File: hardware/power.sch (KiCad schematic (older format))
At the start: 39 parts, among them U200 SY8089AAC, U220 PAM2305CGFADJ, U230 PAM2305CGFADJ, U250 PAM2305CGFADJ, U260 NCP707_XDFN4

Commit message: wip
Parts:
- added L251: 2.2u,0806, require:L_0806, symbol Device:L
- C201, C221, C231: value 10u -> 10u,10V; footprint require:C_0603 -> require:C_0805
- C202, C222, C232, C252: value 22p -> 100p
- C210: value 0.1u -> 10n
- C223, C233: value 22u -> 10u
- C251: value 2.2u,10V -> 10u,10V; footprint require:C_0603 -> require:C_0805
- C253: value 22u -> 10u,10V; footprint require:C_0603 -> require:C_0805
- L230: value 0.47u,3A -> 2.2u
- L250: value 0.47u,3A -> 2.2u,0806
- R201: value 100R,1% -> 100R
- R210: value 10k -> 169k,1%
- R232: value 110k,1% -> 150k,1%
- R233: value 150k,1% -> 100k,1%
- R252: value 110k,1% -> 540k,1%
- R253: value 150k,1% -> 120k,1%
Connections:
- net +3V3: now also L251.2
- net at L250.1, U250.4 (SW): now also L251.1
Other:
- note added: "1.04V"
- note removed: "CORE"
- note removed: "Murata DFE252012R-H-2R2M#\n"
- note removed: "Use TI TLV713 DQN"
- moved on the sheet: C200, C201, C202, C203, C204, C210, R201, R202, R203, R210, R211, R212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

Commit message: wip
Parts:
- L220: value 0.47u,3A -> 2.2u
- L250, L251: value 2.2u,0806 -> 2.2u
- U260: value NCP707_XDFN4 -> NCP707CMX180TCG
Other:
- note added: "1.5V"
- note added: "3.3V"
- moved on the sheet: C201, C202, C203, C204, C210, C221, C222, C223, C231, C232, C233, C251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

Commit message: wip
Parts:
- removed C251: 10u,10V, require:C_0805, symbol require-rescue:C
- added C251: 10u,10V, require:C_0805, symbol Device:C
- C201, C221, C231: symbol require-rescue:C -> Device:C
- C253: Type (none) -> X5R; Voltage (none) -> 10V
- L200: footprint require:L_murata_2520 -> require:L_1008
- R203, R222, R223, R232, R233, R252, R253: symbol require-rescue:R -> Device:R
- U200: footprint TO_SOT_Packages_SMD:SOT-23-5 -> require:SOT-23-5
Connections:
- net +5V: now also C251.1
- net GND: now also C251.2
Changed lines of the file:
@@
 F 0 "L200" V 3850 1300 50  0000 C CNN
 F 1 "2.2u" V 3950 1300 50  0000 C CNN
-F 2 "require:L_murata_2520" V 4050 1300 50  0000 C CNN
+F 2 "require:L_1008" V 4050 1300 50  0000 C CNN
 F 3 "" H 3750 1300 50  0001 C CNN
 	1    3750 1300
@@
 F 0 "U200" H 3125 2047 60  0000 C CNN
 F 1 "SY8089AAC" H 3125 1941 60  0000 C CNN
-F 2 "TO_SOT_Packages_SMD:SOT-23-5" H 2950 1550 60  0001 C CNN
+F 2 "require:SOT-23-5" H 2950 1550 60  0001 C CNN
 F 3 "" H 2950 1550 60  0001 C CNN
 	1    2950 1550
@@
 $EndComp
 $Comp
-L require-rescue:R R203
+L Device:R R203
 U 1 1 5CCCBB88
 P 4100 2550
@@
 	9750 1300 9750 1400
 $Comp
-L require-rescue:R R222
+L Device:R R222
 U 1 1 5CD090A3
 P 8550 1550
@@
 	8250 1300 8550 1300
 $Comp
-L require-rescue:R R223
+L Device:R R223
 U 1 1 5CD090B6
 P 8550 2050
@@
 $EndComp
 $Comp
-L require-rescue:C C221
+L Device:C C221
 U 1 1 5CD9D5EF
 P 6300 1550
@@
 $EndComp
 $Comp
-L require-rescue:C C231
+L Device:C C231
 U 1 1 5C6A4C06
 P 6300 3300
@@
 $EndComp
 $Comp
-L require-rescue:C C201
+L Device:C C201
 U 1 1 5C6A4C90
 P 1400 1550
@@
 $EndComp
 $Comp
-L require-rescue:C C251
-U 1 1 5CA6F70F
-P 6300 5100
-AR Path="/5C2CD8AE/5CA6F70F" Ref="C251"  Part="1"
-AR Path="/5C325762/5CA6F70F" Ref="C?"  Part="1"
-F 0 "C251" H 6400 5150 50  0000 L CNN
-F 1 "10u,10V" H 6400 5050 50  0000 L CNN
-F 2 "require:C_0805" H 6338 4950 50  0000 C CNN
-F 3 "" H 6300 5100 50  0001 C CNN
-	1    6300 5100
-	1    0    0    -1
-$EndComp
-$Comp
 L power:GND #PWR0232
 U 1 1 5CA8588D
@@
 	9750 3050 9750 3150
 $Comp
-L require-rescue:R R232
+L Device:R R232
 U 1 1 5C7EE8E1
 P 8550 3300
@@
 	8250 3050 8550 3050
 $Comp
-L require-rescue:R R233
+L Device:R R233
 U 1 1 5C7EE8E9
 P 8550 3800
@@
 	8100 3250 8100 3550
 $Comp
-L Device:C C253
-U 1 1 5C868D3A
-P 9750 5100
-AR Path="/5C2CD8AE/5C868D3A" Ref="C253"  Part="1"
-AR Path="/5C325762/5C868D3A" Ref="C?"  Part="1"
-F 0 "C253" H 9850 5150 50  0000 L CNN
-F 1 "10u,10V" H 9850 5050 50  0000 L CNN
-F 2 "require:C_0805" H 9850 4950 50  0000 C CNN
-F 3 "" H 9750 5100 50  0001 C CNN
-	1    9750 5100
-	1    0    0    -1
-$EndComp
-$Comp
 L require-rescue:GND #PWR0166
 U 1 1 5C868D41
@@
 	9750 4850 9750 4950
 $Comp
-L require-rescue:R R252
+L Device:R R252
 U 1 1 5C868D49
 P 8550 5100
@@
 $EndComp
 $Comp
-L require-rescue:R R253
+L Device:R R253
 U 1 1 5C868D51
 P 8550 5600
@@
 Text Notes 9150 4800 0    50   ~ 0
 3.3V
+$Comp
+L Device:C C251
+U 1 1 5C988A95
+P 6300 5100
+AR Path="/5C2CD8AE/5C988A95" Ref="C251"  Part="1"
+AR Path="/5C325762/5C988A95" Ref="C?"  Part="1"
+AR Path="/5C2F0873/5C988A95" Ref="C?"  Part="1"
+F 0 "C251" H 6400 5150 50  0000 L CNN
+F 1 "10u,10V" H 6400 5050 50  0000 L CNN
+F 2 "require:C_0805" H 6400 4950 50  0000 C CNN
+F 3 "" H 6300 5100 50  0001 C CNN
+F 4 "10V" H 6300 5100 60  0001 C CNN "Voltage"
+F 5 "X5R" H 6300 5100 60  0001 C CNN "Type"
+	1    6300 5100
+	1    0    0    -1
+$EndComp
+$Comp
+L Device:C C253
+U 1 1 5C988E54
+P 9750 5100
+AR Path="/5C2CD8AE/5C988E54" Ref="C253"  Part="1"
+AR Path="/5C325762/5C988E54" Ref="C?"  Part="1"
+AR Path="/5C2F0873/5C988E54" Ref="C?"  Part="1"
+F 0 "C253" H 9850 5150 50  0000 L CNN
+F 1 "10u,10V" H 9850 5050 50  0000 L CNN
+F 2 "require:C_0805" H 9850 4950 50  0000 C CNN
+F 3 "" H 9750 5100 50  0001 C CNN
+F 4 "10V" H 9750 5100 60  0001 C CNN "Voltage"
+F 5 "X5R" H 9750 5100 60  0001 C CNN "Type"
+	1    9750 5100
+	1    0    0    -1
+$EndComp
 $EndSCHEMATC

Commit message: wip
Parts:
- removed L251: 2.2u, require:L_0806, symbol Device:L
- removed U250: PAM2305CGFADJ, require:U-DFN2020-6, symbol Regulator_Switching:PAM2305CGFADJ
- added C254: 10u,10V, require:C_0805, symbol Device:C
- added U250: SY8089AAC, require:SOT-23-5, symbol require:SY8089AAC
- L250: footprint require:L_0806 -> require:L_1008
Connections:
- net +3V3: now also C254.1
- net +5V: now also U250.1 (EN), U250.4 (VIN)
- net GND: now also C254.2, U250.2 (GND)
- net at L250.1: now also U250.3 (LX)
- net at C252.2, R252.2, R253.1: now also U250.5 (FB)
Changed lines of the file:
@@
-$EndComp
-$Comp
-L power:GND #PWR0232
-U 1 1 5CA8588D
-P 7350 5350
-F 0 "#PWR0232" H 7350 5100 50  0001 C CNN
-F 1 "GND" H 7355 5177 50  0000 C CNN
-F 2 "" H 7350 5350 50  0001 C CNN
-F 3 "" H 7350 5350 50  0001 C CNN
-	1    7350 5350
-	1    0    0    -1
 $EndComp
 $Comp
@@
 F 0 "L250" V 8200 4850 50  0000 C CNN
 F 1 "2.2u" V 8300 4850 50  0000 C CNN
-F 2 "require:L_0806" V 8200 4450 50  0000 C CNN
+F 2 "require:L_1008" V 8200 4450 50  0000 C CNN
 F 3 "" H 8100 4850 50  0001 C CNN
 	1    8100 4850
@@
 	1    0    0    -1
 $EndComp
-$Comp
-L Regulator_Switching:PAM2305CGFADJ U250
-U 1 1 5C7DD750
-P 7450 4950
-F 0 "U250" H 7450 5317 50  0000 C CNN
-F 1 "PAM2305CGFADJ" H 7450 5226 50  0000 C CNN
-F 2 "require:U-DFN2020-6" H 7500 4700 50  0001 L CNN
-F 3 "https://www.diodes.com/assets/Datasheets/PAM2305.pdf" H 7200 4600 50  0001 C CNN
-	1    7450 4950
-	1    0    0    -1
-$EndComp
-Wire Wire Line
-	7050 4850 6850 4850
 Wire Wire Line
 	6300 4850 6300 4750
@@
 $EndComp
 Wire Wire Line
-	7050 5050 6850 5050
-Wire Wire Line
 	6850 5050 6850 4850
 Connection ~ 6850 4850
 Wire Wire Line
 	6850 4850 6300 4850
-Wire Wire Line
-	7950 4850 7900 4850
-$Comp
-L power:GND #PWR0248
-U 1 1 5C8012B7
-P 7450 5350
-F 0 "#PWR0248" H 7450 5100 50  0001 C CNN
-F 1 "GND" H 7455 5177 50  0000 C CNN
-F 2 "" H 7450 5350 50  0001 C CNN
-F 3 "" H 7450 5350 50  0001 C CNN
-	1    7450 5350
-	1    0    0    -1
-$EndComp
-Wire Wire Line
-	7450 5250 7450 5350
-Wire Wire Line
-	7350 5250 7350 5350
 $Comp
 L power:GND #PWR0107
@@
 Connection ~ 9750 4850
 Wire Wire Line
-	8250 4850 8300 4850
-Wire Wire Line
 	7850 5050 8100 5050
 Wire Wire Line
@@
 	1    0    0    -1
 $EndComp
-$Comp
-L Device:L L251
-U 1 1 5C82D93D
-P 8100 4500
-AR Path="/5C2CD8AE/5C82D93D" Ref="L251"  Part="1"
-AR Path="/5C325762/5C82D93D" Ref="L?"  Part="1"
-AR Path="/5C2F0873/5C82D93D" Ref="L?"  Part="1"
-F 0 "L251" V 8200 4500 50  0000 C CNN
-F 1 "2.2u" V 8300 4500 50  0000 C CNN
-F 2 "require:L_0806" V 8200 4100 50  0000 C CNN
-F 3 "" H 8100 4500 50  0001 C CNN
-	1    8100 4500
-	0    -1   -1   0
-$EndComp
-Wire Wire Line
-	8250 4500 8300 4500
-Wire Wire Line
-	8300 4500 8300 4850
-Connection ~ 8300 4850
-Wire Wire Line
-	8300 4850 8550 4850
-Wire Wire Line
-	7950 4500 7900 4500
-Wire Wire Line
-	7900 4500 7900 4850
-Connection ~ 7900 4850
-Wire Wire Line
-	7900 4850 7850 4850
 Connection ~ 4700 1800
 Wire Wire Line
@@
 	1    0    0    -1
 $EndComp
+$Comp
+L require:SY8089AAC U250
+U 1 1 5CCB83FE
+P 7300 5100
+AR Path="/5C2CD8AE/5CCB83FE" Ref="U250"  Part="1"
+AR Path="/5C325762/5CCB83FE" Ref="U?"  Part="1"
+F 0 "U250" H 7475 5597 60  0000 C CNN
+F 1 "SY8089AAC" H 7475 5491 60  0000 C CNN
+F 2 "require:SOT-23-5" H 7300 5100 60  0001 C CNN
+F 3 "" H 7300 5100 60  0001 C CNN
+	1    7300 5100
+	1    0    0    -1
+$EndComp
+Wire Wire Line
+	6850 4850 7100 4850
+Wire Wire Line
+	6850 5050 7100 5050
+$Comp
+L power:GND #PWR0222
+U 1 1 5CCC88FD
+P 7000 4950
+F 0 "#PWR0222" H 7000 4700 50  0001 C CNN
+F 1 "GND" V 7005 4822 50  0000 R CNN
+F 2 "" H 7000 4950 50  0001 C CNN
+F 3 "" H 7000 4950 50  0001 C CNN
+	1    7000 4950
+	0    1    1    0
+$EndComp
+Wire Wire Line
+	7000 4950 7100 4950
+Wire Wire Line
+	8250 4850 8550 4850
+Wire Wire Line
+	7850 4850 7950 4850
+$Comp
+L Device:C C254
+U 1 1 5CCDA7D4
+P 10400 5100
+AR Path="/5C2CD8AE/5CCDA7D4" Ref="C254"  Part="1"
+AR Path="/5C325762/5CCDA7D4" Ref="C?"  Part="1"
+AR Path="/5C2F0873/5CCDA7D4" Ref="C?"  Part="1"
+F 0 "C254" H 10500 5150 50  0000 L CNN
+F 1 "10u,10V" H 10500 5050 50  0000 L CNN
+F 2 "require:C_0805" H 10500 4950 50  0000 C CNN
+F 3 "" H 10400 5100 50  0001 C CNN
+F 4 "10V" H 10400 5100 60  0001 C CNN "Voltage"
+F 5 "X5R" H 10400 5100 60  0001 C CNN "Type"
+	1    10400 5100
+	1    0    0    -1
+$EndComp
+Wire Wire Line
+	10400 4850 10400 4950
+Wire Wire Line
+	10400 5250 10400 5400
+$Comp
+L power:GND #PWR0223
+U 1 1 5CCE4B67
+P 10400 5400
+F 0 "#PWR0223" H 10400 5150 50  0001 C CNN
+F 1 "GND" H 10405 5227 50  0000 C CNN
+F 2 "" H 10400 5400 50  0001 C CNN
+F 3 "" H 10400 5400 50  0001 C CNN
+	1    10400 5400
+	1    0    0    -1
+$EndComp
+Wire Wire Line
+	9750 4850 10400 4850
 $EndSCHEMATC

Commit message: wip
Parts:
- removed R201: 100R, require:R_0402, symbol Device:R
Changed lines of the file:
@@
 	5100 1300 5100 1400
-$Comp
-L Device:R R201
-U 1 1 5CCCBB6C
-P 4100 1550
-AR Path="/5C2CD8AE/5CCCBB6C" Ref="R201"  Part="1"
-AR Path="/5C325762/5CCCBB6C" Ref="R?"  Part="1"
-F 0 "R201" H 4200 1600 50  0000 L CNN
-F 1 "100R" H 4200 1500 50  0000 L CNN
-F 2 "require:R_0402" V 4030 1550 50  0001 C CNN
-F 3 "" H 4100 1550 50  0001 C CNN
-	1    4100 1550
-	1    0    0    -1
-$EndComp
 $Comp
 L Device:R R202
@@
 	1    0    0    -1
 $EndComp
-Wire Wire Line
-	4100 1300 4100 1400
-Wire Wire Line
-	4100 1300 4700 1300
 $Comp
 L require:SY8089AAC U200
@@
 $EndComp
 Wire Wire Line
-	4100 1700 4100 1800
-Wire Wire Line
 	4700 1800 4100 1800
-Connection ~ 4100 1800
 Wire Wire Line
 	4700 2200 4700 2300
@@
 	3600 1300 3500 1300
 Wire Wire Line
-	3900 1300 4100 1300
-Connection ~ 4100 1300
-Wire Wire Line
 	3750 2300 4100 2300
 Connection ~ 3750 2300
@@
 Wire Wire Line
 	9750 4850 10400 4850
+Wire Wire Line
+	3900 1300 4700 1300
 $EndSCHEMATC

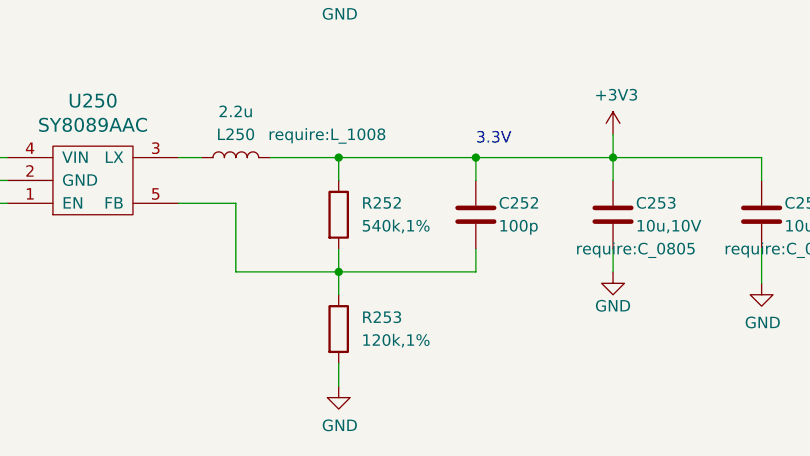
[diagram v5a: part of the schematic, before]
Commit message: update bom, change 3.3V divider resistor value
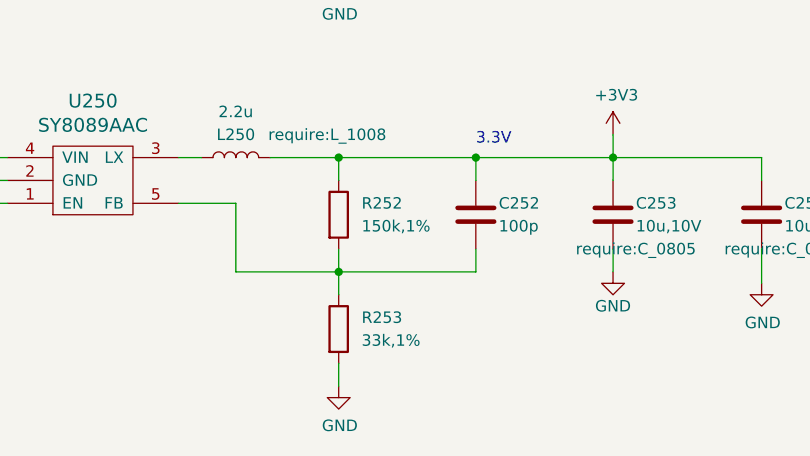
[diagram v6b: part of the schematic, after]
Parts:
- R252: value 540k,1% -> 150k,1%
- R253: value 120k,1% -> 33k,1%
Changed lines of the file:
@@
 AR Path="/5C325762/5C868D49" Ref="R?"  Part="1"
 F 0 "R252" H 8650 5150 50  0000 L CNN
-F 1 "540k,1%" H 8650 5050 50  0000 L CNN
+F 1 "150k,1%" H 8650 5050 50  0000 L CNN
 F 2 "require:R_0402" V 8480 5100 50  0001 C CNN
 F 3 "" H 8550 5100 50  0001 C CNN
@@
 AR Path="/5C325762/5C868D51" Ref="R?"  Part="1"
 F 0 "R253" H 8650 5650 50  0000 L CNN
-F 1 "120k,1%" H 8650 5550 50  0000 L CNN
+F 1 "33k,1%" H 8650 5550 50  0000 L CNN
 F 2 "require:R_0402" V 8480 5600 50  0001 C CNN
 F 3 "" H 8550 5600 50  0001 C CNN
